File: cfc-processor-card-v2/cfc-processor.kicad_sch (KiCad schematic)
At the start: 11 parts, among them J1 TFM-120-01-L-D-RA, J2 2-1734592-0, J3 J-SAMTEC-TFM-110-X1-XXX-D-RA, J4 Conn_01x04

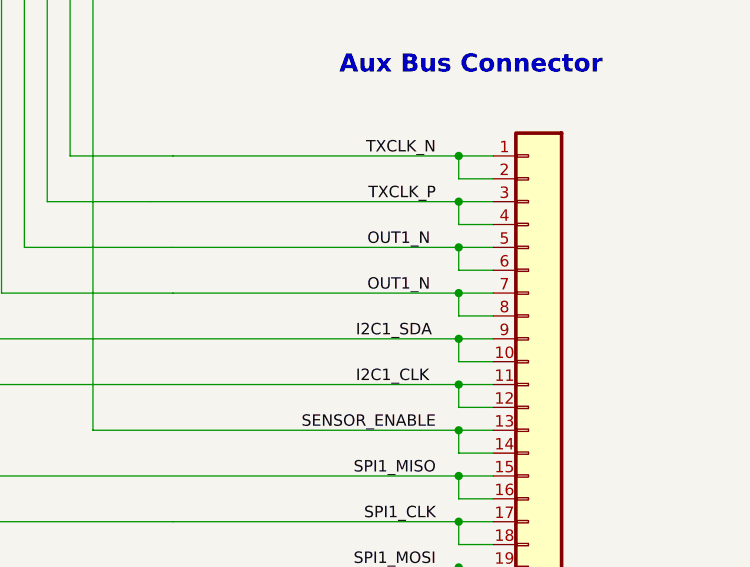
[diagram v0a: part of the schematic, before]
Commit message: Update
updated opd address resistors to 100 ohms from 100 ohms, changed the 100 ohm res VBUSP to 10 ohms. Updated TEC page for sensor to have bidirectional current sense for diag. Removed misc testpoints
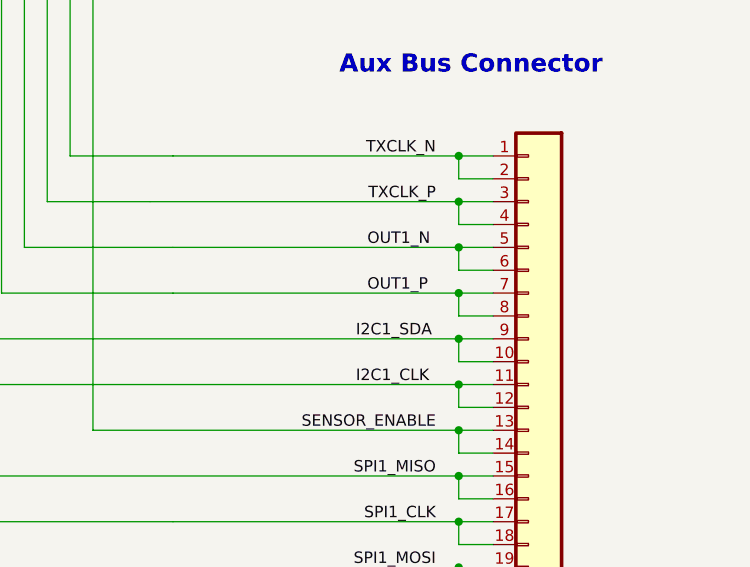
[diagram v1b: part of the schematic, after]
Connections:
- net OUT1_N: no longer J3.7, J3.8
- new net OUT1_P: J3.7, J3.8
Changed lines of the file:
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@@
 		)
 	)
-	(label "OUT1_N"
+	(label "OUT1_P"
 		(at 378.46 142.24 0)
 		(effects

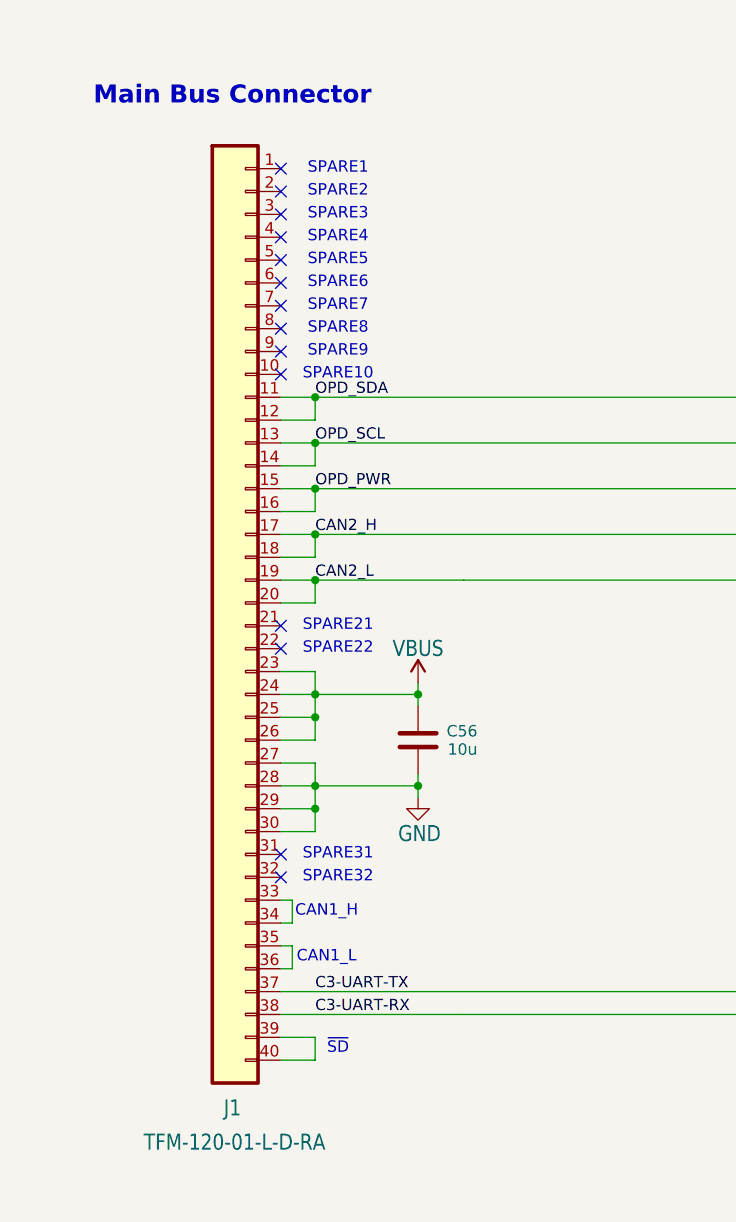
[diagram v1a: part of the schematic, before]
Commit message: Processor board routing
Completed rework and routing of processor board. No drc errors or warnings. Ready for design review on processor board. Minor changes to schematic for easier routing on pull down resistors connected to the octavo SIP. Reannotated sensor schematic component designators.
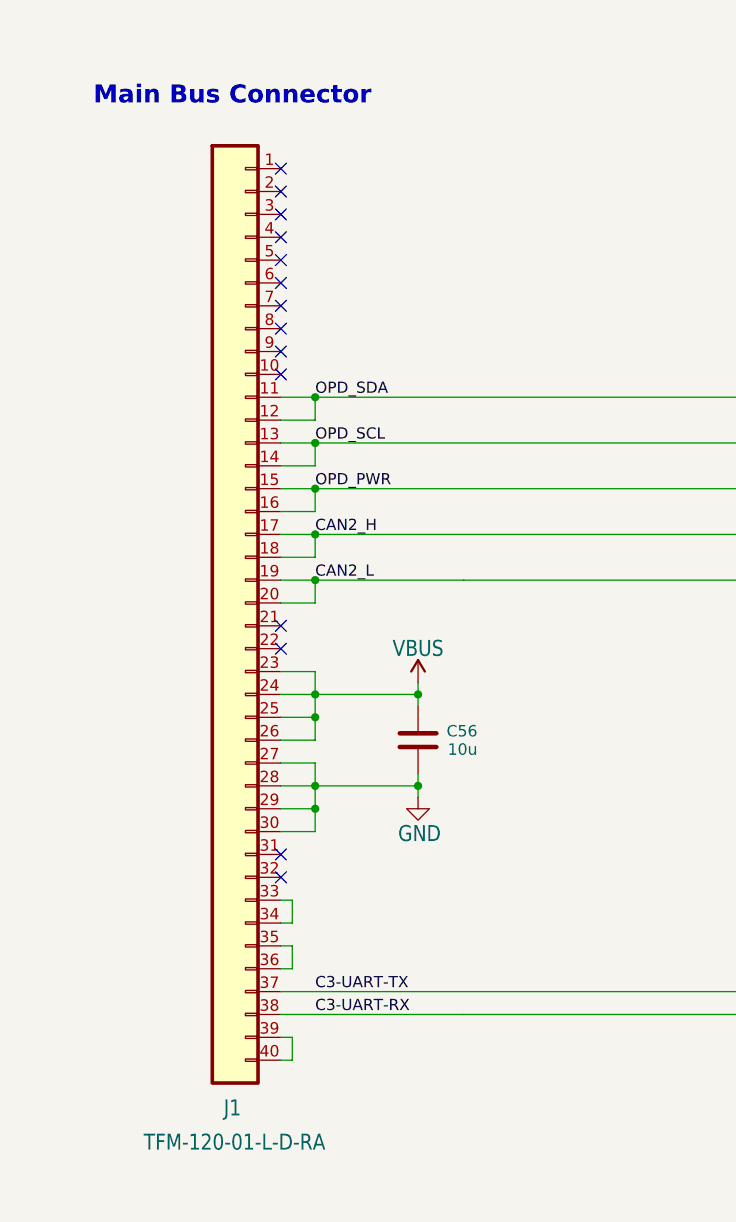
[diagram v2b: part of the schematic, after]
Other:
- note removed: "CAN1_H"
- note removed: "CAN1_L"
- note removed: "SPARE1"
- note removed: "SPARE10"
- note removed: "SPARE2"
- note removed: "SPARE21"
- note removed: "SPARE22"
- note removed: "SPARE3"
- note removed: "SPARE31"
- note removed: "SPARE32"
- note removed: "SPARE4"
- note removed: "SPARE5"
- note removed: "SPARE6"
- note removed: "SPARE7"
- note removed: "SPARE8"
- note removed: "SPARE9"
- note removed: "~{SD}"
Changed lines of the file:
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@@
 		(company "Portland State Aerospace Society")
-	)
-	(text "SPARE8"
-		(exclude_from_sim no)
-		(at 49.53 49.53 0)
-		(effects
-			(font
-				(size 1.27 1.27)
-			)
-		)
-	)
-	(text "SPARE9"
-		(exclude_from_sim no)
-		(at 49.53 52.07 0)
-		(effects
-			(font
-				(size 1.27 1.27)
-			)
-		)
-	)
-	(text "SPARE1"
-		(exclude_from_sim no)
-		(at 49.53 31.75 0)
-		(effects
-			(font
-				(size 1.27 1.27)
-			)
-		)
 	)
 	(text "Bill of Materials is kept in a Google Sheet Here:\nhttps://docs.google.com/spreadsheets/d/11vG1kWyrAjmbF5QJM-EhXmvQoF6O47japwYlHF802do/edit#gid=668351130"
@@
 		)
 	)
-	(text "~{SD}"
-		(exclude_from_sim no)
-		(at 49.53 129.54 0)
-		(effects
-			(font
-				(size 1.27 1.27)
-			)
-		)
-	)
-	(text "SPARE4"
-		(exclude_from_sim no)
-		(at 49.53 39.37 0)
-		(effects
-			(font
-				(size 1.27 1.27)
-			)
-		)
-	)
-	(text "SPARE3"
-		(exclude_from_sim no)
-		(at 49.53 36.83 0)
-		(effects
-			(font
-				(size 1.27 1.27)
-			)
-		)
-	)
 	(text "EEPROM Programming Jumper\n\nPull Pin 3 low to write to EEPROM.\nUse Raspberry Pi Pico board with\nCircuit Python software to program.\n\nCareful with ESD!"
 		(exclude_from_sim no)
@@
 			)
 			(justify left bottom)
-		)
-	)
-	(text "SPARE7"
-		(exclude_from_sim no)
-		(at 49.53 46.99 0)
-		(effects
-			(font
-				(size 1.27 1.27)
-			)
-		)
-	)
-	(text "SPARE31"
-		(exclude_from_sim no)
-		(at 49.53 107.95 0)
-		(effects
-			(font
-				(size 1.27 1.27)
-			)
-		)
-	)
-	(text "CAN1_H"
-		(exclude_from_sim no)
-		(at 48.26 114.3 0)
-		(effects
-			(font
-				(size 1.27 1.27)
-			)
-		)
-	)
-	(text "SPARE5"
-		(exclude_from_sim no)
-		(at 49.53 41.91 0)
-		(effects
-			(font
-				(size 1.27 1.27)
-			)
-		)
-	)
-	(text "SPARE21"
-		(exclude_from_sim no)
-		(at 49.53 82.55 0)
-		(effects
-			(font
-				(size 1.27 1.27)
-			)
-		)
-	)
-	(text "CAN1_L"
-		(exclude_from_sim no)
-		(at 48.26 119.38 0)
-		(effects
-			(font
-				(size 1.27 1.27)
-			)
 		)
 	)
@@
 		)
 	)
-	(text "SPARE10"
-		(exclude_from_sim no)
-		(at 49.53 54.61 0)
-		(effects
-			(font
-				(size 1.27 1.27)
-			)
-		)
-	)
 	(text "Main Bus Connector"
 		(exclude_from_sim no)
@@
 		)
 	)
-	(text "SPARE32"
-		(exclude_from_sim no)
-		(at 49.53 110.49 0)
-		(effects
-			(font
-				(size 1.27 1.27)
-			)
-		)
-	)
 	(text "Oresat Debug Connector"
 		(exclude_from_sim no)
@@
 		)
 	)
-	(text "SPARE6"
-		(exclude_from_sim no)
-		(at 49.53 44.45 0)
-		(effects
-			(font
-				(size 1.27 1.27)
-			)
-		)
-	)
-	(text "SPARE2"
-		(exclude_from_sim no)
-		(at 49.53 34.29 0)
-		(effects
-			(font
-				(size 1.27 1.27)
-			)
-		)
-	)
-	(text "SPARE22"
-		(exclude_from_sim no)
-		(at 49.53 85.09 0)
-		(effects
-			(font
-				(size 1.27 1.27)
-			)
-		)
-	)
 	(junction
 		(at 46.99 72.39)
@@
 	(wire
 		(pts
-			(xy 46.99 128.27) (xy 43.18 128.27)
+			(xy 44.45 128.27) (xy 43.18 128.27)
 		)
 		(stroke
@@
 	(wire
 		(pts
-			(xy 46.99 130.81) (xy 46.99 128.27)
+			(xy 44.45 130.81) (xy 44.45 128.27)
 		)
 		(stroke
@@
 	(wire
 		(pts
-			(xy 43.18 130.81) (xy 46.99 130.81)
-		)
-		(stroke
+			(xy 43.18 130.81) (xy 44.45 130.81)
+		)
+		(stroke
